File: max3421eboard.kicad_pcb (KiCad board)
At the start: 2 copper layers, 41.3 x 48.9 mm, 32 parts, among them J1 USB A, J2 USB MicroB, J3 1x10, J4 1x8, J5 1x8, J6 1x3, J7 Conn_01x04, U1 MAX3421E, U2 LP2985-3.3, U3 STMPS2141STR, Y1 12MHz

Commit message: Update board layout
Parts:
- J2: footprint Connectors:USB_Micro-B_10103594-0001LF -> Connector_USB:USB_Micro-B_Molex-105017-0001
- Y1: footprint Crystals:Crystal_SMD_5032-2pin_5.0x3.2mm_HandSoldering -> Crystal:Crystal_HC49-4H_Vertical
- moved Y1 2.29 mm to (32.8, 68.6)
- moved REF*** 0.89 mm to (45.1, 65.8)
- moved J2 0.51 mm to (24.8, 49.7)
- moved C1 0.51 mm to (27.9, 64.9)
- moved C2 0.51 mm to (33.0, 64.9)
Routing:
- net /X-: track 18.4 -> 17.5 mm
- net GND: track 34.4 -> 33.6 mm

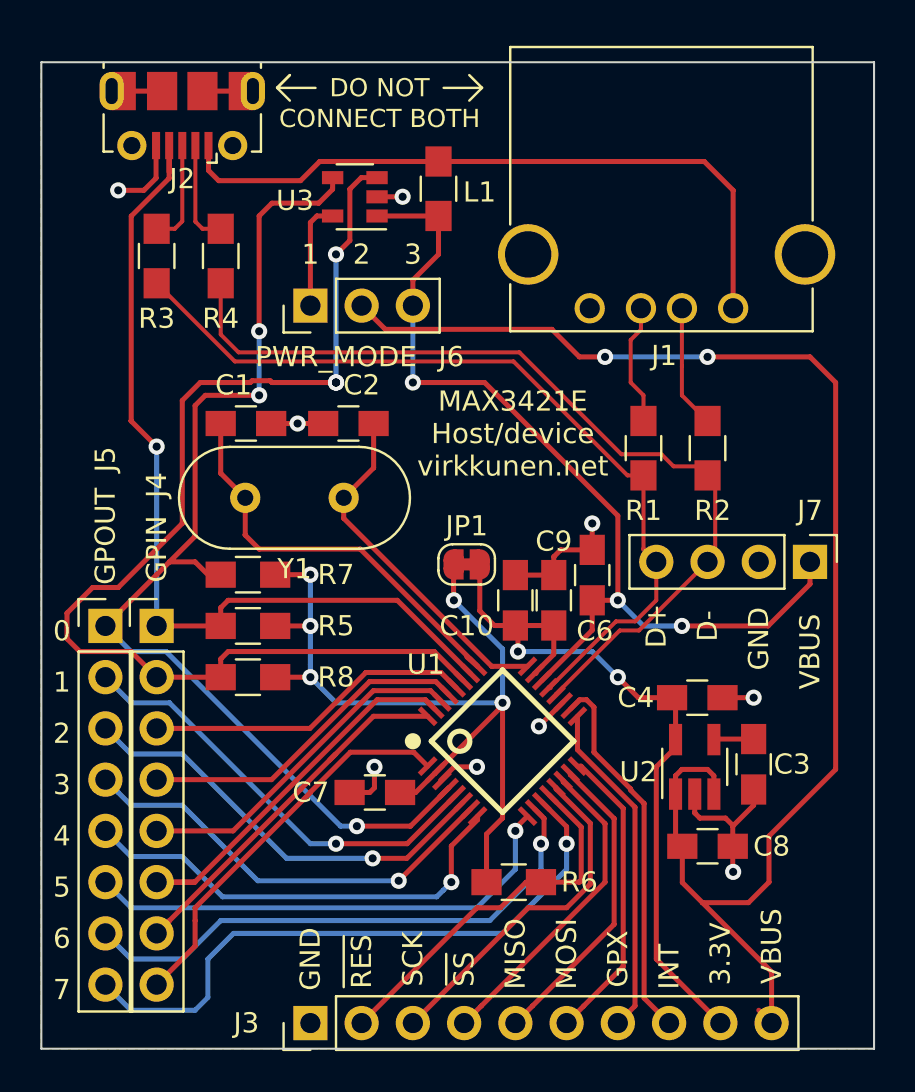
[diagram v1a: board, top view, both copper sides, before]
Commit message: Align board to the 1mm grid
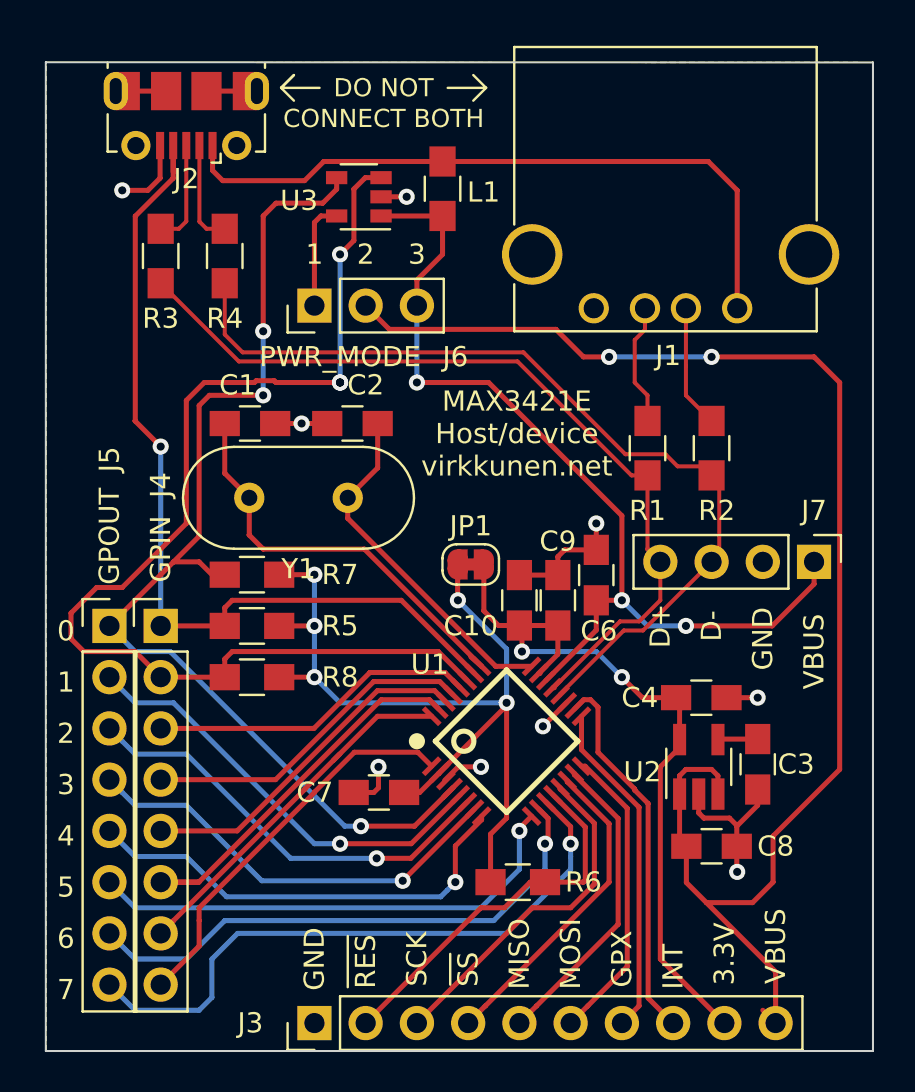
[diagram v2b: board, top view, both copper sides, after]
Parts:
- moved C10 0.20 mm to (41.5, 73.7)
- moved C2 0.20 mm to (33.2, 64.9)
- moved C3 0.20 mm to (53.3, 81.8)
- moved C8 0.20 mm to (51.0, 85.9)
- moved C9 0.20 mm to (43.4, 73.7)
- moved J1 0.20 mm to (52.3, 59.2)
- moved J3 0.20 mm to (31.3, 94.6)
- moved J5 0.20 mm to (21.2, 74.9)
- moved J6 0.20 mm to (31.3, 59.1)
- moved R1 0.20 mm to (47.8, 66.1)
- moved R2 0.20 mm to (51.0, 66.1)
- moved R6 0.20 mm to (41.4, 87.6)
- moved U1 0.20 mm to (40.8, 80.6)
- moved U2 0.20 mm to (50.4, 81.9)
- moved U3 0.20 mm to (33.5, 53.7)
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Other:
- board size 41.3 x 48.9 mm -> 41 x 49 mm

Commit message: Fix the board layout
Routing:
- net /X+: track 21.0 -> 20.3 mm

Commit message: Use Rezonit solder mask parameters
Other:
- rule pad_to_mask_clearance: 0.051 -> 0.05
- rule solder_mask_min_width: 0.25 -> 0.145
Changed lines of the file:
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@@
     (pad_size 1.524 1.524)
     (pad_drill 0.762)
-    (pad_to_mask_clearance 0.051)
-    (solder_mask_min_width 0.25)
+    (pad_to_mask_clearance 0.05)
+    (solder_mask_min_width 0.145)
     (aux_axis_origin 18 47)
     (visible_elements FFFFFF7F)

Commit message: Fix the board layout
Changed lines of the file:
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@@
       (drillshape 0)
       (scaleselection 1)
-      (outputdirectory ""))
+      (outputdirectory "out-my/"))
   )
   (net 0 "")
@@
   )
   (gr_line (start 59 47) (end 59 96) (layer Edge.Cuts) (width 0.1))
-  (gr_line (start 18 46.99) (end 59 47) (layer Edge.Cuts) (width 0.1))
-  (gr_line (start 18 96) (end 18 46.99) (layer Edge.Cuts) (width 0.1))
+  (gr_line (start 18 47) (end 59 47) (layer Edge.Cuts) (width 0.1))
+  (gr_line (start 18 96) (end 18 47) (layer Edge.Cuts) (width 0.1))
   (segment (start 23.665 51.665) (end 23.695 51.435) (width 0.25) (layer F.Cu) (net 1))
   (segment (start 23.665 51.465) (end 23.695 51.435) (width 0.25) (layer F.Cu) (net 1))
@@
     (polygon
       (pts
-        (xy 59 96) (xy 18 96) (xy 18 46.99) (xy 59 47)
+        (xy 59 96) (xy 18 96) (xy 18 47) (xy 59 47)
       )
     )
